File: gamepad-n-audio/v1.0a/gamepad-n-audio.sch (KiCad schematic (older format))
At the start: 35 parts, among them J1 5V, J2 Switchcraft_35RAPC4BHN3, J3 Gamepads, J4 PMOD, J5 jmp, U1 74LVC2T45, U2 74LVC2T45, U3 74LVC2T45, U4 74AUP2G3404, U5 74AUP2G3404

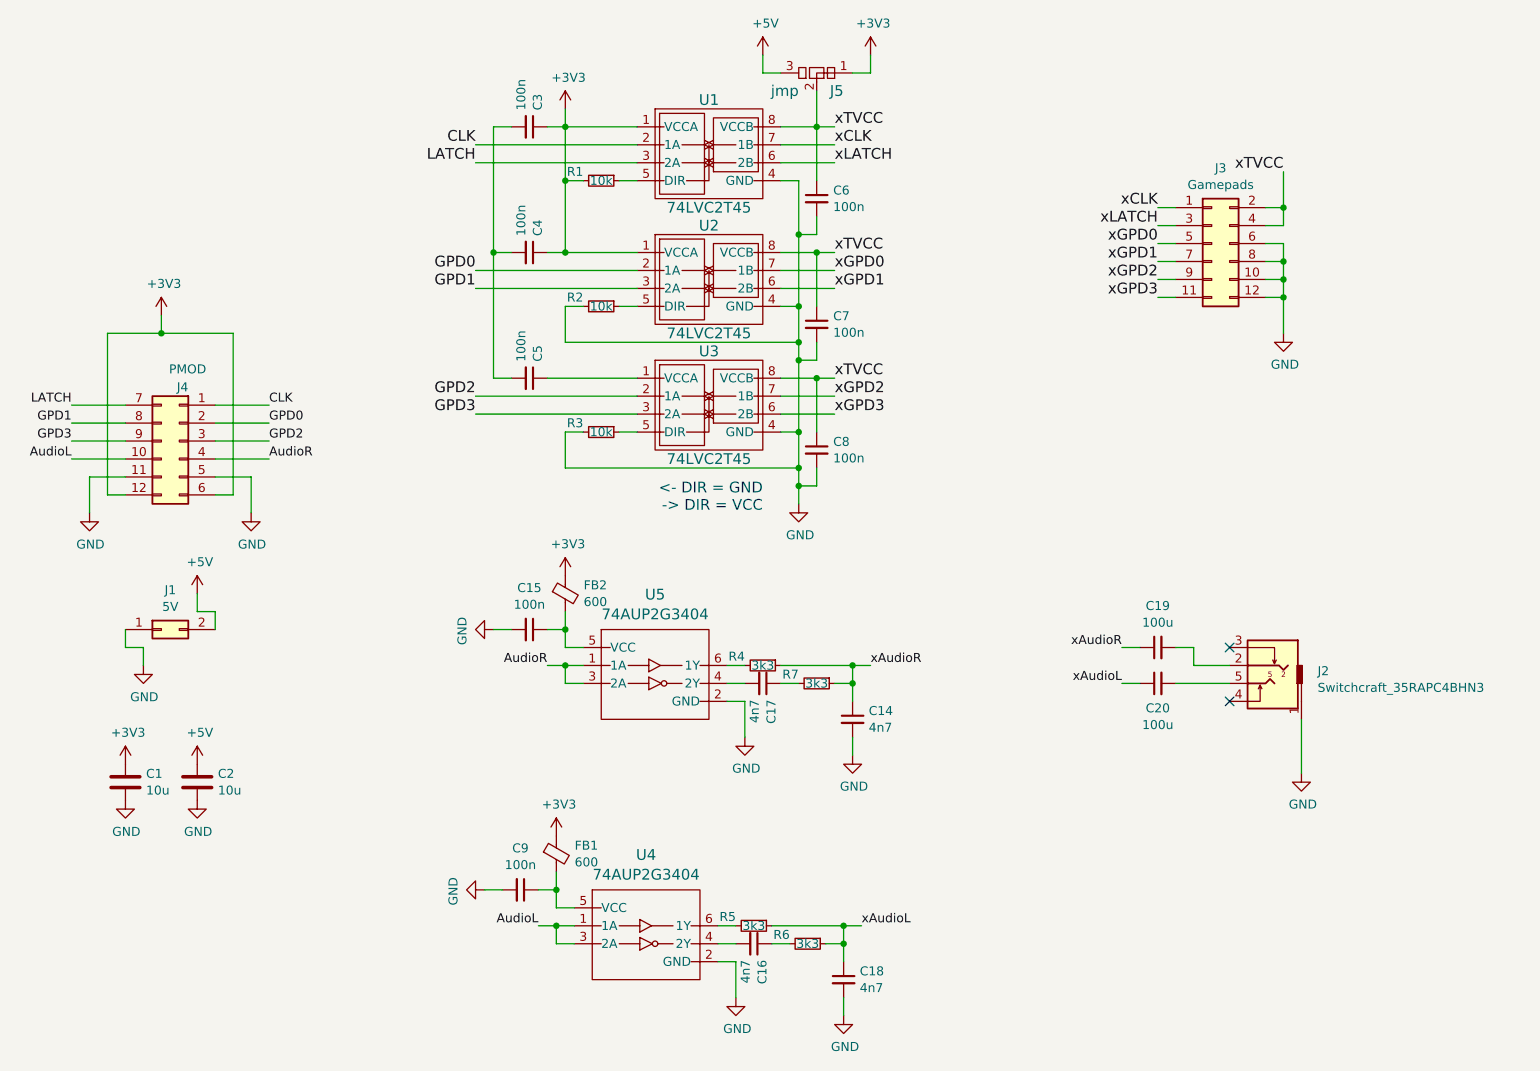
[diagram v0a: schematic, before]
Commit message: Finished first routing pass on the gamepad & audio Pmod.
This is the status of the board after the Twitch stream on April 16th.
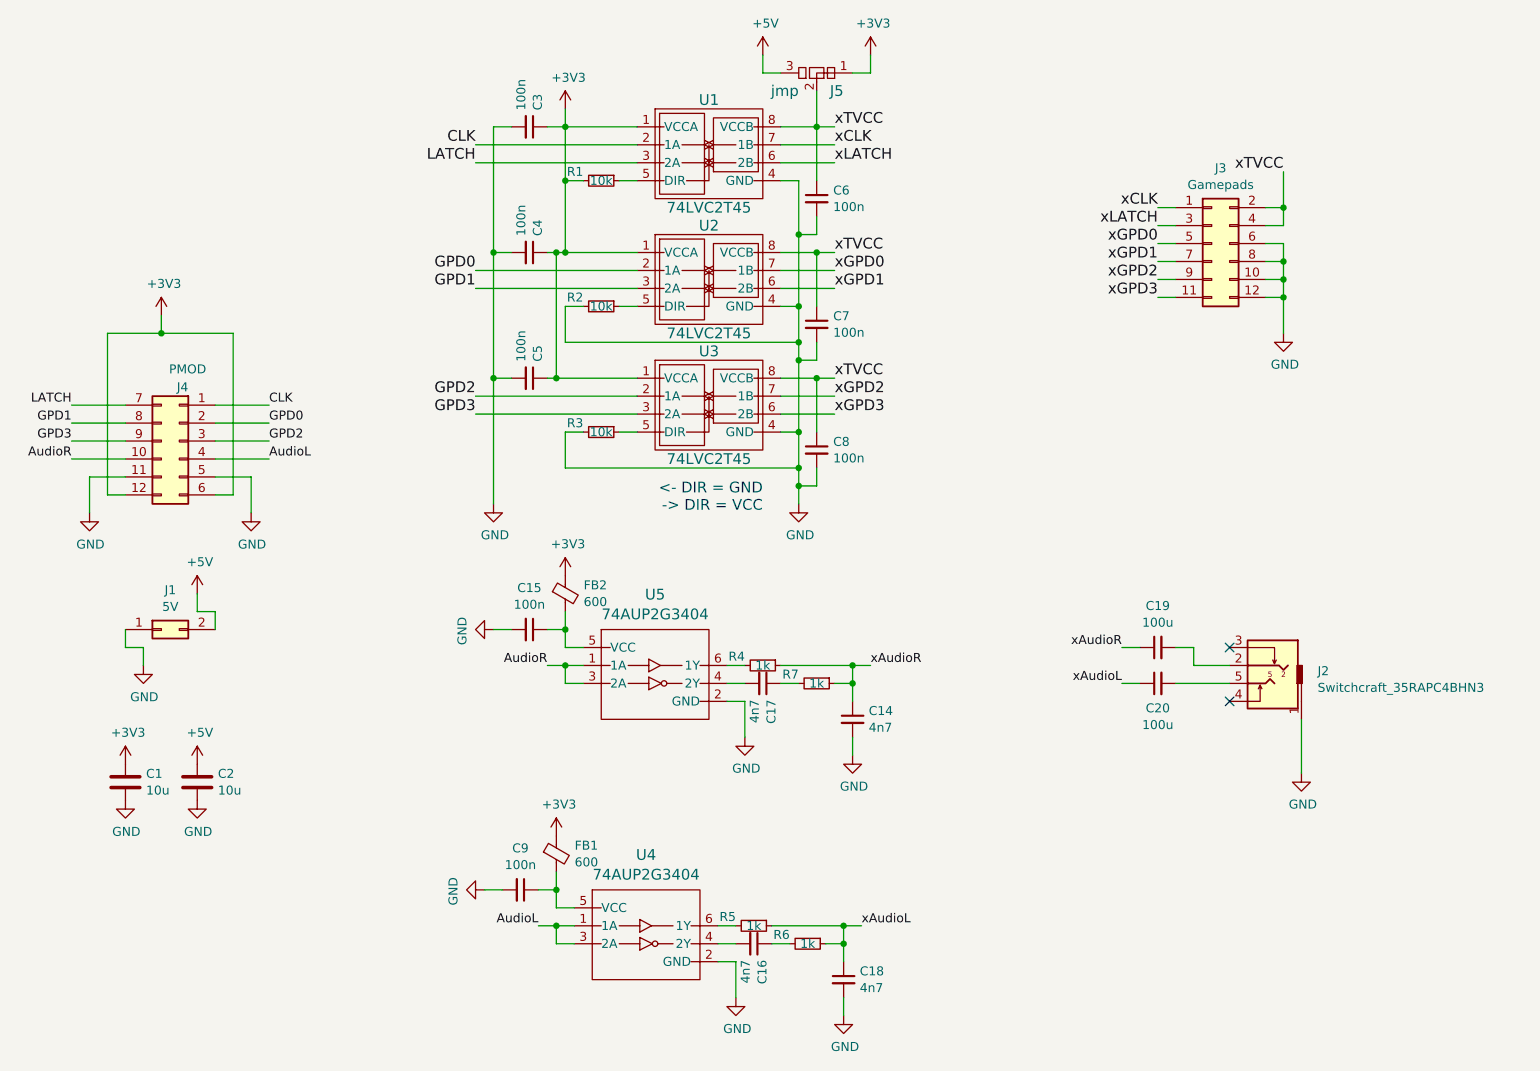
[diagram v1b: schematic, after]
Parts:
- R4, R5, R6, R7: value 3k3 -> 1k
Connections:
- net +3V3: now also C5.1, U3.1 (VCCA)
- net AudioL: now also J4.4 (Pin_4); no longer J4.10 (Pin_10)
- net AudioR: now also J4.10 (Pin_10); no longer J4.4 (Pin_4)
- net GND: now also C3.2, C4.2, C5.2
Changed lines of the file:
@@
 Text Label 800  3400 2    50   ~ 0
 GPD3
-Text Label 800  3500 2    50   ~ 0
+Text Label 1900 3500 0    50   ~ 0
 AudioL
 Text Label 1900 3400 0    50   ~ 0
 GPD2
-Text Label 1900 3500 0    50   ~ 0
+Text Label 800  3500 2    50   ~ 0
 AudioR
 Wire Wire Line
@@
 	4950 1650 4950 1950
 Wire Wire Line
-	3450 2350 3550 2350
+	3450 2350 3500 2350
 Connection ~ 3550 1650
 Connection ~ 3550 2350
@@
 xCLK
 Wire Wire Line
-	3450 3050 3950 3050
+	3450 3050 3500 3050
 Wire Wire Line
 	3550 2650 3550 2850
@@
 P 4650 4650
 F 0 "R4" V 4600 4550 50  0000 R CNN
-F 1 "3k3" V 4650 4650 50  0000 C CNN
+F 1 "1k" V 4650 4650 50  0000 C CNN
 F 2 "pkl_dipol:R_0402" H 4591 4559 60  0001 R CNN
 F 3 "" H 4650 4650 60  0000 C CNN
@@
 P 4950 4750
 F 0 "R7" V 4900 4650 50  0000 R CNN
-F 1 "3k3" V 4950 4750 50  0000 C CNN
+F 1 "1k" V 4950 4750 50  0000 C CNN
 F 2 "pkl_dipol:R_0402" H 4891 4659 60  0001 R CNN
 F 3 "" H 4950 4750 60  0000 C CNN
@@
 P 4600 6100
 F 0 "R5" V 4550 6000 50  0000 R CNN
-F 1 "3k3" V 4600 6100 50  0000 C CNN
+F 1 "1k" V 4600 6100 50  0000 C CNN
 F 2 "pkl_dipol:R_0402" H 4541 6009 60  0001 R CNN
 F 3 "" H 4600 6100 60  0000 C CNN
@@
 P 4900 6200
 F 0 "R6" V 4850 6100 50  0000 R CNN
-F 1 "3k3" V 4900 6200 50  0000 C CNN
+F 1 "1k" V 4900 6200 50  0000 C CNN
 F 2 "pkl_dipol:R_0402" H 4841 6109 60  0001 R CNN
 F 3 "" H 4900 6200 60  0000 C CNN
@@
 	7550 2200 7550 2100
 Connection ~ 7550 2100
+Wire Wire Line
+	3500 3050 3500 2350
+Connection ~ 3500 3050
+Wire Wire Line
+	3500 3050 3950 3050
+Connection ~ 3500 2350
+Wire Wire Line
+	3500 2350 3550 2350
+Wire Wire Line
+	3150 3050 3150 3750
+Connection ~ 3150 3050
+$Comp
+L power:GND #PWR0115
+U 1 1 5E9C01FD
+P 3150 3750
+F 0 "#PWR0115" H 3150 3500 50  0001 C CNN
+F 1 "GND" H 3158 3576 50  0000 C CNN
+F 2 "" H 3150 3750 50  0000 C CNN
+F 3 "" H 3150 3750 50  0000 C CNN
+	1    3150 3750
+	1    0    0    -1
+$EndComp
 $EndSCHEMATC
